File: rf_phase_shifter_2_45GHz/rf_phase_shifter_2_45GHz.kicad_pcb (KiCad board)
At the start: 2 copper layers, 53.5 x 21 mm, 16 parts, among them J1 CON-SMA-EDGE-S, J2 CON-SMA-EDGE-S, J3 CON-SMA-EDGE-S

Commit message: update
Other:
- board text added: "Analog RF phase shifter 2.45 GHz Marcin Wachowiak, Poland"
- board text removed: "Analog RF phase shifter 2.45GHz Marcin Wachowiak, Poland"

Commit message: added info about substrate thickness
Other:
- board text added: "Substrate: FR4, thickness: 0.6 mm"

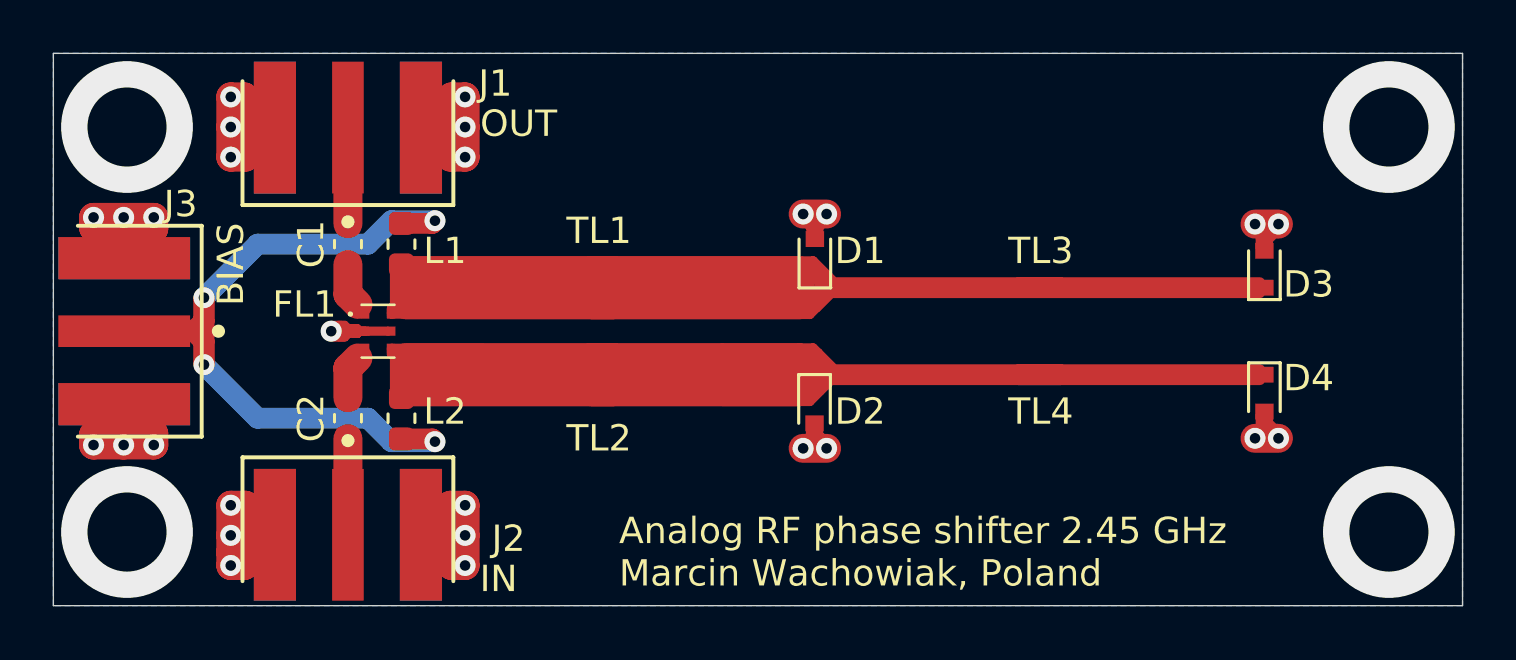
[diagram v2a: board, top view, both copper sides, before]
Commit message: Finished layout of second prototypes
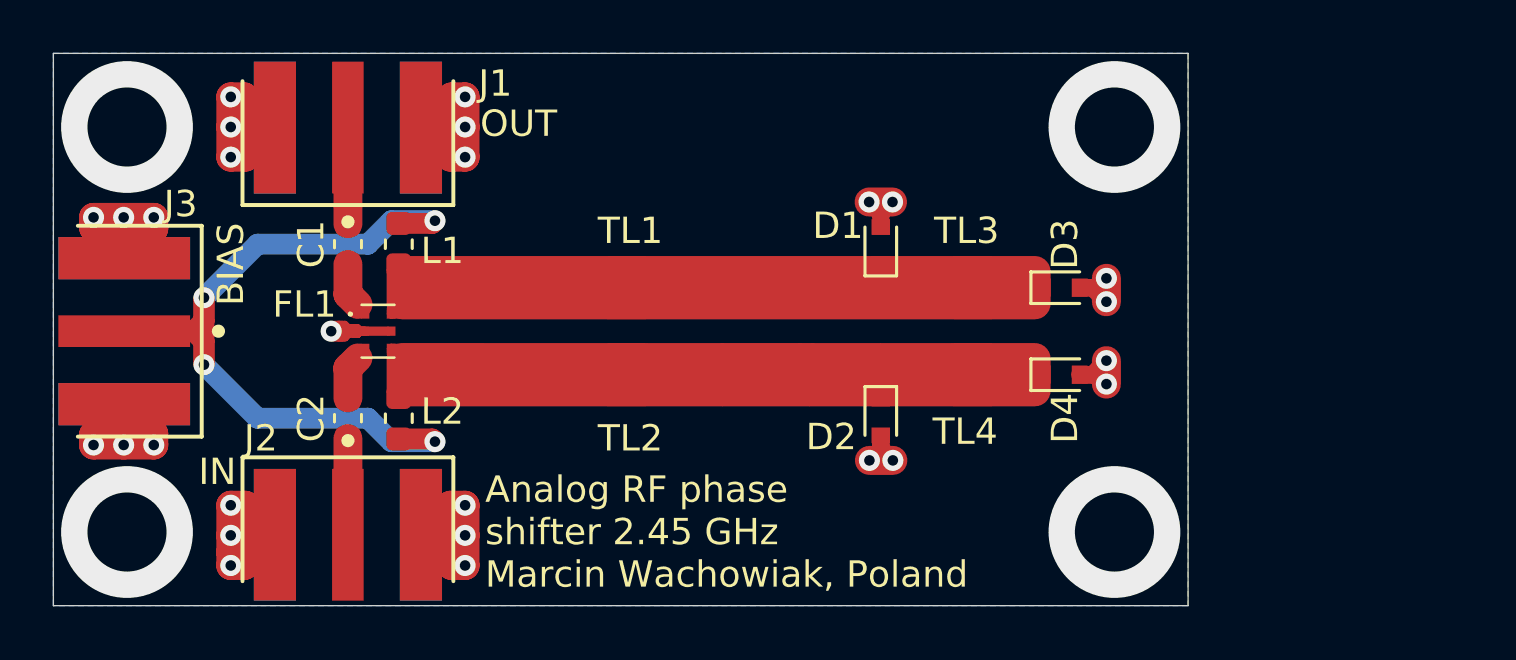
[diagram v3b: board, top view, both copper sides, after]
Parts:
- D1, D2, D3, D4: value BBY66_02V -> SMV1763-079LF
- moved D3 7.74 mm to (111.5, 57.3), turned to 0 degrees
- moved D4 7.74 mm to (111.5, 60.6), turned to 0 degrees
- moved TL3 2.81 mm to (107.9, 57.3)
- moved TL4 2.81 mm to (107.9, 60.6)
- moved D2 2.56 mm to (104.7, 62.2)
- moved D1 2.54 mm to (104.7, 55.7)
- moved TL1 1.19 mm to (95.3, 57.3)
- moved TL2 1.19 mm to (95.3, 60.6)
- moved L1 0.10 mm to (86.4, 55.6)
- moved L2 0.10 mm to (86.4, 62.2)
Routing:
- net Net-(D1-Pad1): track 30.5 -> 16.8 mm
- net Net-(D2-Pad1): track 46.8 -> 36.2 mm
- net Net-(D4-Pad1): track 8.48 -> 0.00 mm
- net Net-(D3-Pad1): track 4.75 -> 0.00 mm
- net GND: track 69.4 -> 70.1 mm
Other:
- board size 53.5 x 21 mm -> 43.1 x 21 mm
